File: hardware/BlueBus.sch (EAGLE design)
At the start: 74 parts

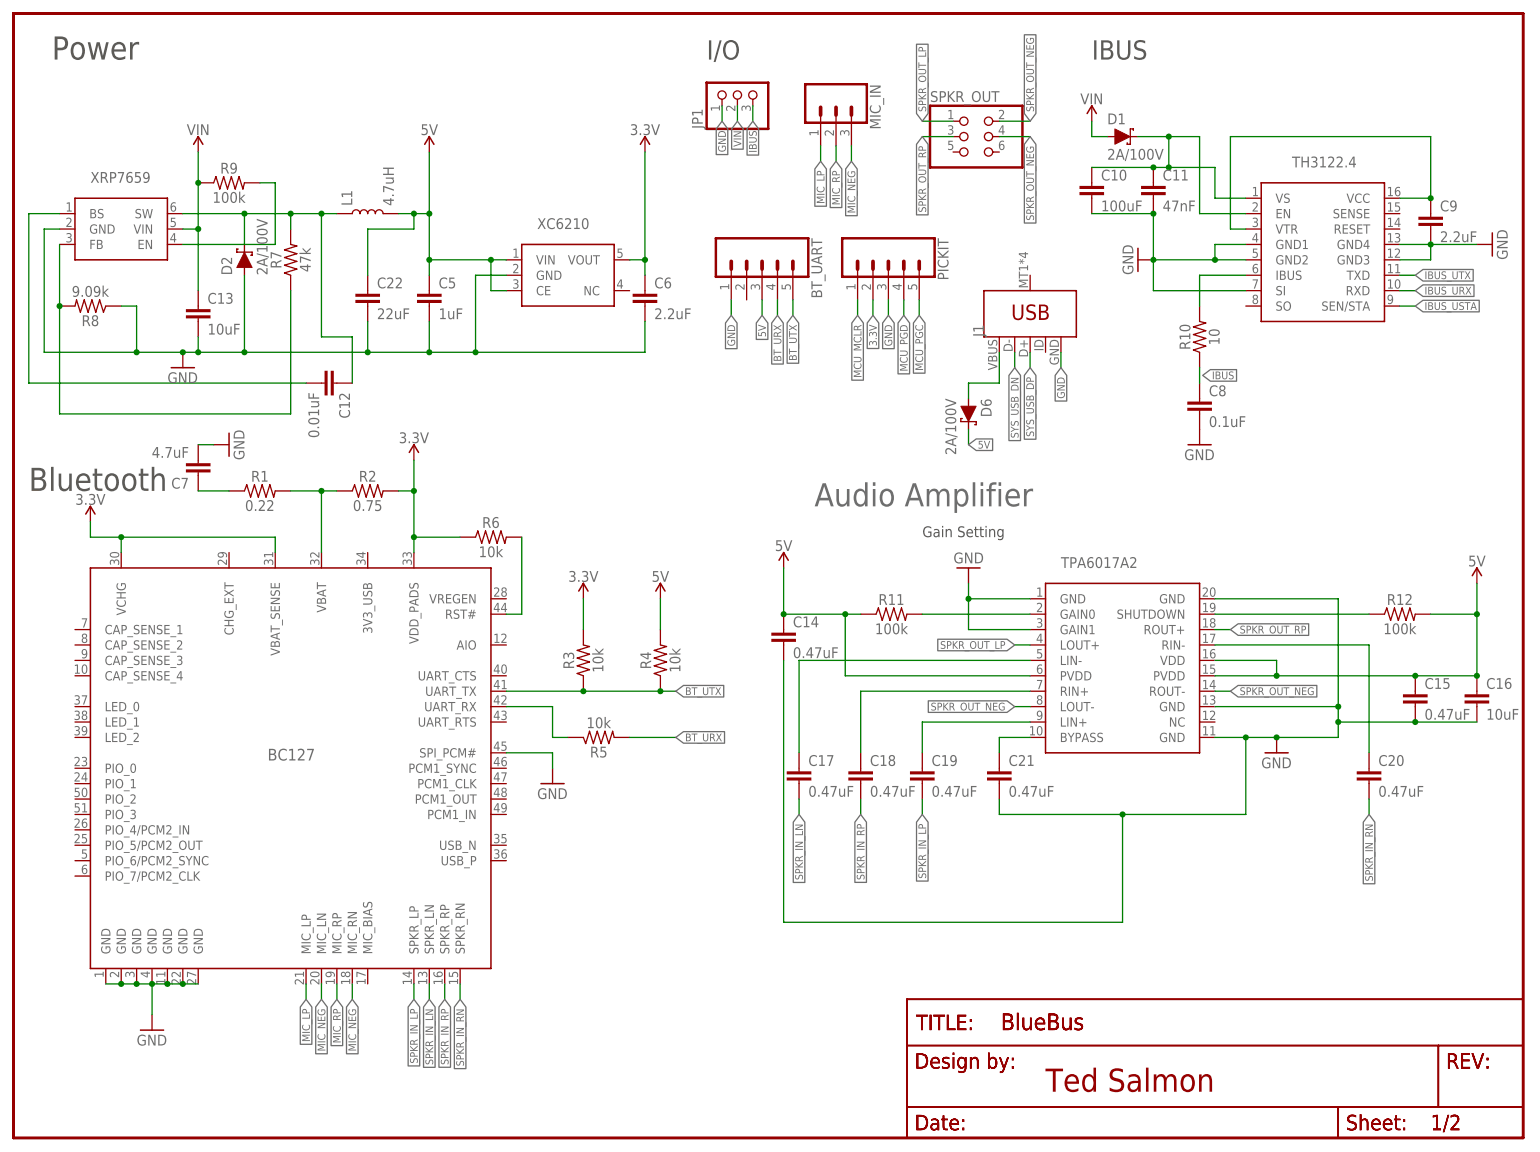
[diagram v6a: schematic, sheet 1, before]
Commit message: [ADD] hardware: BlueBus v6 * Version bump for new PCB run * Remove passives from IBus line causing I/O issues * Rewire gain settings on TPA6017A2 to 10dB gain, rather than 15.7dB * Ensure all vias are 0.51mm * Add Thermal Pad (PWP) to TPA6017A2 and update footprint to make more sense in mm * Rewire VIN * Rewire 5v regulator BS pin to pull from 5v rail rather than SW line (pre-inductor) per the DS
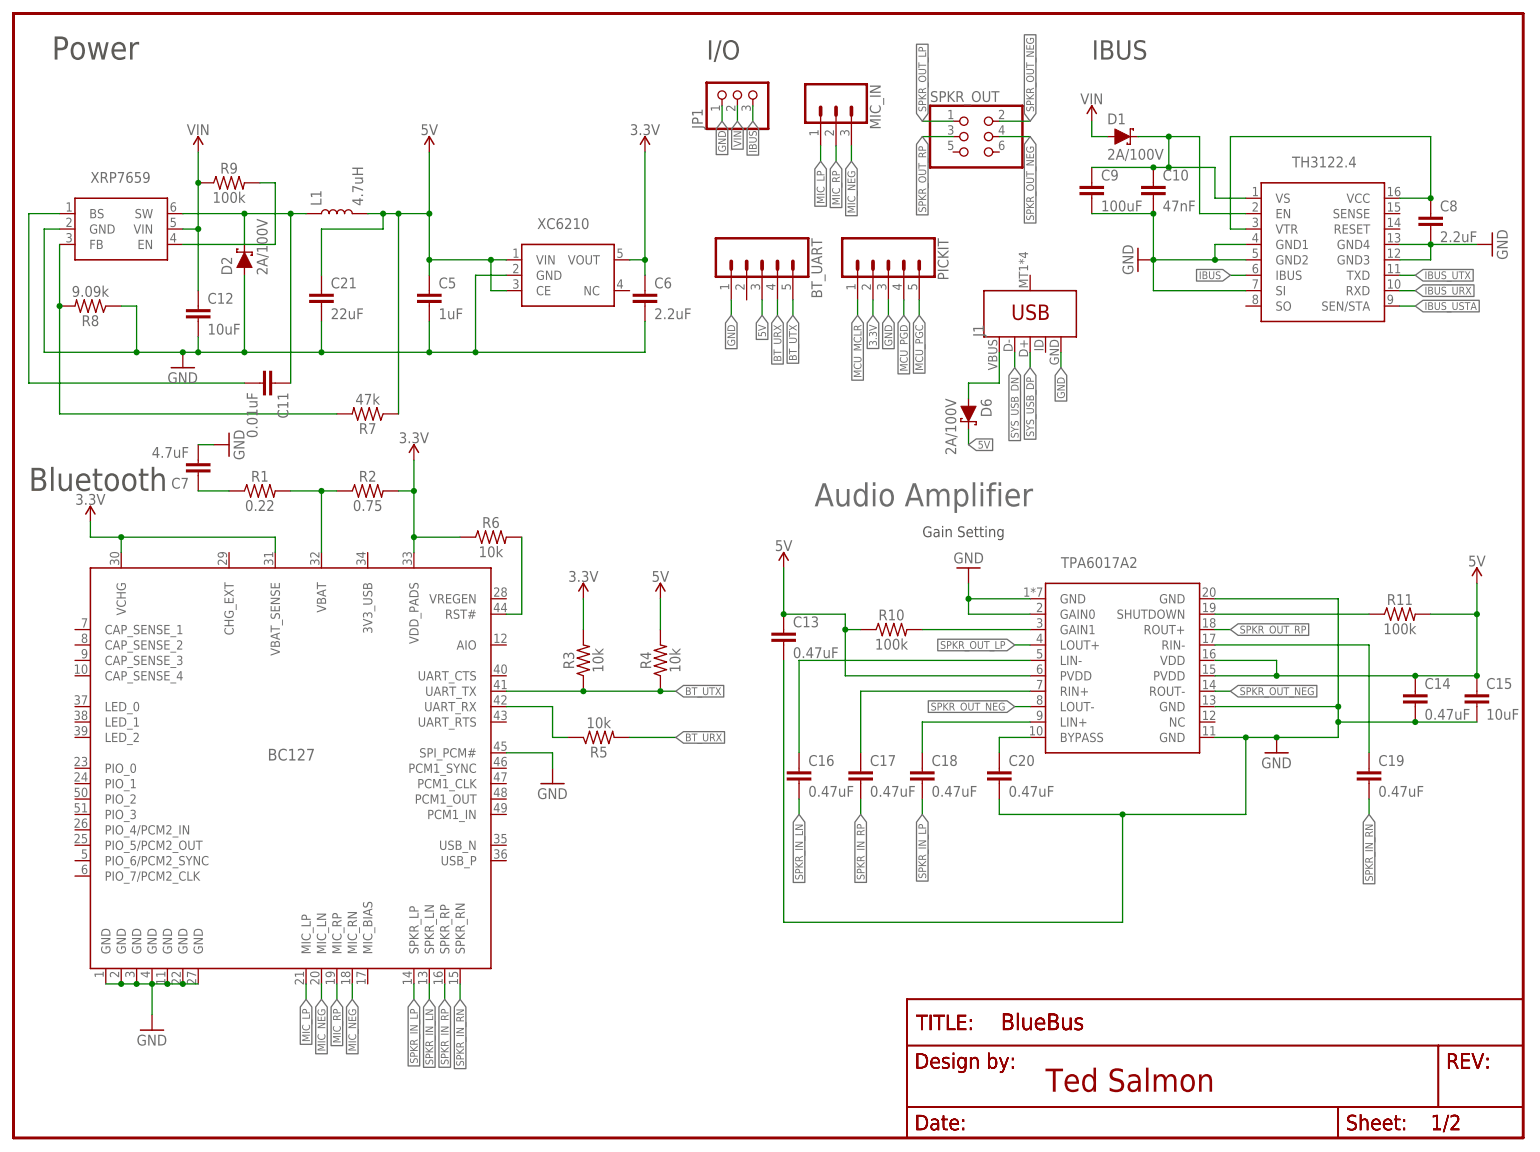
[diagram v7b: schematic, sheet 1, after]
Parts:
- removed C28: 0.1uF, Passives:0.1UF
- removed R22: 240, Passives:240OHM
- C10: value 100uF -> 47nF; device Passives:100UF2917 -> Passives:47NF
- C11: value 47nF -> 0.01uF; device Passives:47NF -> Passives:0.01UF
- C12: value 0.01uF -> 10uF; device Passives:0.01UF -> Passives:10UF
- C13, C16: value 10uF -> 0.47uF; device Passives:10UF -> Passives:0.47UF
- C15: value 0.47uF -> 10uF; device Passives:0.47UF -> Passives:10UF
- C21: value 0.47uF -> 22uF; device Passives:0.47UF -> Passives:22UF
- C22: value 22uF -> 0.1uF; device Passives:22UF -> Passives:0.1UF
- C26: value 0.1uF -> 10uF; device Passives:0.1UF -> Passives:10UF
- C27: value 10uF -> 0.1uF; device Passives:10UF -> Passives:0.1UF
- C8: value 0.1uF -> 2.2uF; device Passives:0.1UF -> Passives:2.2UF
- C9: value 2.2uF -> 100uF; device Passives:2.2UF -> Passives:100UF2917
- R10: value 10 -> 100k; device Passives:10OHM -> Passives:100KOHM0805
- R14: value 100k -> 1k; device Passives:100KOHM0805 -> Passives:1KOHM
- R16: value 1k -> 10k; device Passives:1KOHM -> Passives:10KOHM0805
- R17: value 10k -> 5.1k; device Passives:10KOHM0805 -> Passives:5.1KOHM0805
- R18: value 5.1k -> 36k; device Passives:5.1KOHM0805 -> Passives:36KOHM2012
- R19: value 36k -> 2k; device Passives:36KOHM2012 -> Passives:2KOHM0805
- R20: value 2k -> 10k; device Passives:2KOHM0805 -> Passives:10KOHM0805
- R21: value 10k -> 240; device Passives:10KOHM0805 -> Passives:240OHM
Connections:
- removed net GAIN0: R11.2, TPA6017A2.GAIN0
- removed net IBUS_IN: R10.2, TH3122.IBUS
- new net GAIN1: R10.2, TPA6017A2.GAIN1
- net 3.3V: now also C22.1, R12.1, R16.1, R17.2, R20.1; no longer C25.1, R14.1, R17.1, R18.2, R21.1
- net 5V: now also C13.1, C21.1, R10.1, R11.2, R7.1; no longer C16.1, C22.1, R11.1, R12.2
- net BS: now also C11.2; no longer C12.2
- net BYP: now also C20.1; no longer C21.1
- net EE_CS: now also R17.1; no longer R18.1
- net FB: now also R7.2; no longer R7.1
- net GND: now also C12.2, C20.2, R19.2, TPA6017A2.GAIN0; no longer C11.2, C16.2, C28.2, R20.2, TPA6017A2.GAIN1
- net IBUS: now also TH3122.IBUS; no longer C8.1, R10.1
- net MCP_LED0: now also R15.1; no longer R16.1
- net MCP_LED0_RES: now also R15.2; no longer R16.2
- net MCP_LED1: now also R14.1; no longer R15.1
- net MCP_LED1_RES: now also R14.2; no longer R15.2
- net MCP_RESET: now also R16.2; no longer R17.2
- net MCU_MCLR: now also R21.2; no longer R22.2
- net MCU_MCLR_PULL_UP: now also C27.1, R20.2, R21.1; no longer C28.1, R21.2, R22.1
- net ON_LED: now also R18.1; no longer R19.1
- net ON_LED_RES: now also R18.2, R19.1; no longer R19.2, R20.1
- net SHDN: now also R11.1; no longer R12.1
- net SPKR_IN_LN: now also C16.1, C16.2; no longer C17.1, C17.2
- net SPKR_IN_LP: now also C18.1, C18.2; no longer C19.1, C19.2
- net SPKR_IN_RN: now also C19.1, C19.2; no longer C20.1, C20.2
- net SPKR_IN_RP: now also C17.1, C17.2; no longer C18.1, C18.2
- net SW: now also C11.1; no longer C12.1, R7.2
- net SYS_URX: now also R13.2; no longer R14.2
- net SYS_UTX: now also R12.2; no longer R13.2
- net VCAP: now also C25.1; no longer C27.1
- net VIN: now also C12.1, C9.1; no longer C11.1, C13.1
- net VTR: now also C8.1; no longer C9.1
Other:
- moved on the sheet: C10, C11, C12, C13, C14, C15, C16, C17, C18, C19, C20, C21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
